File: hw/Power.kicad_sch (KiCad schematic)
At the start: 3 parts, among them Q2 SK2302AAT, SW4 SW_SPDT

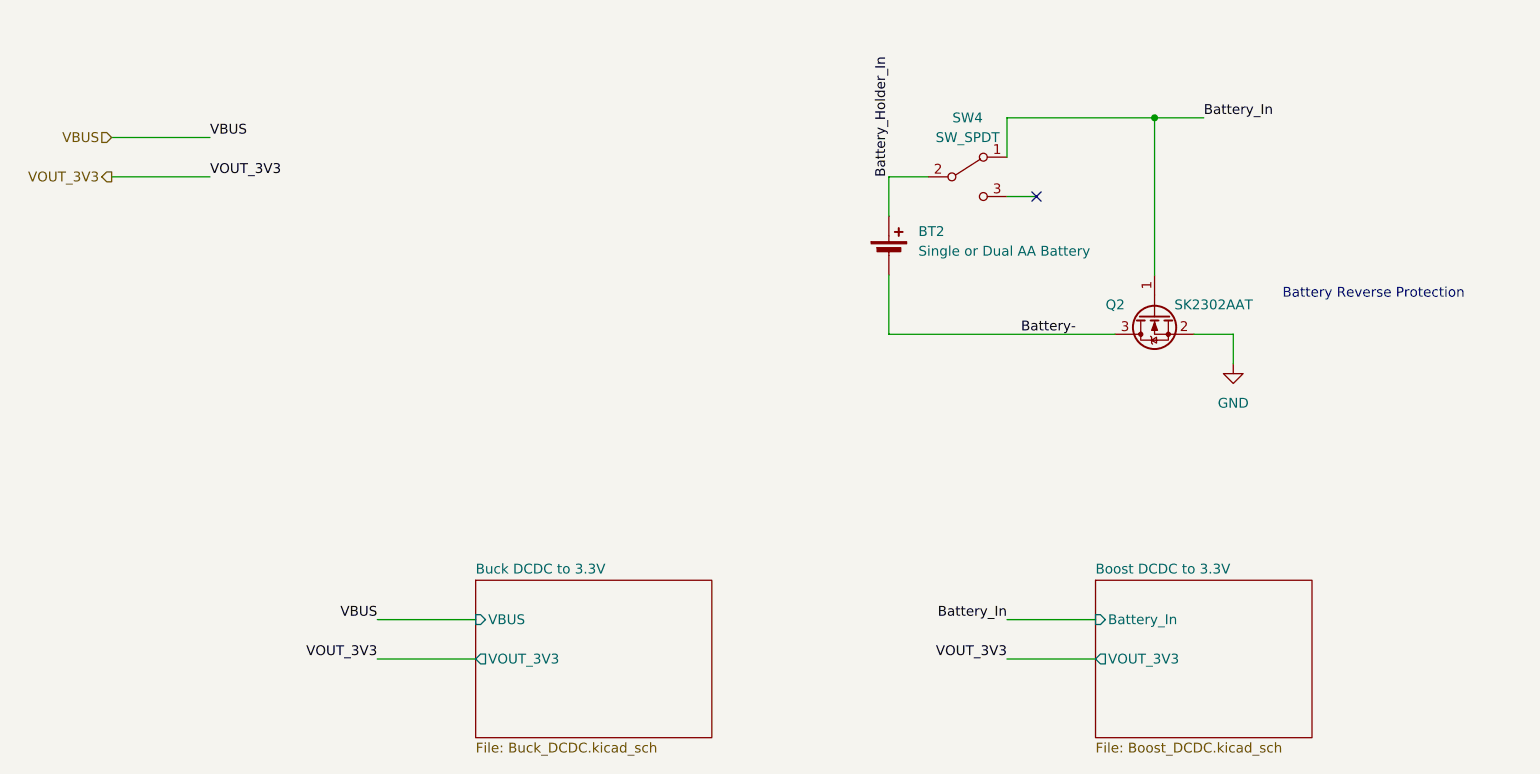
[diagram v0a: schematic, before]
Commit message: wired Battery measurement to ADC
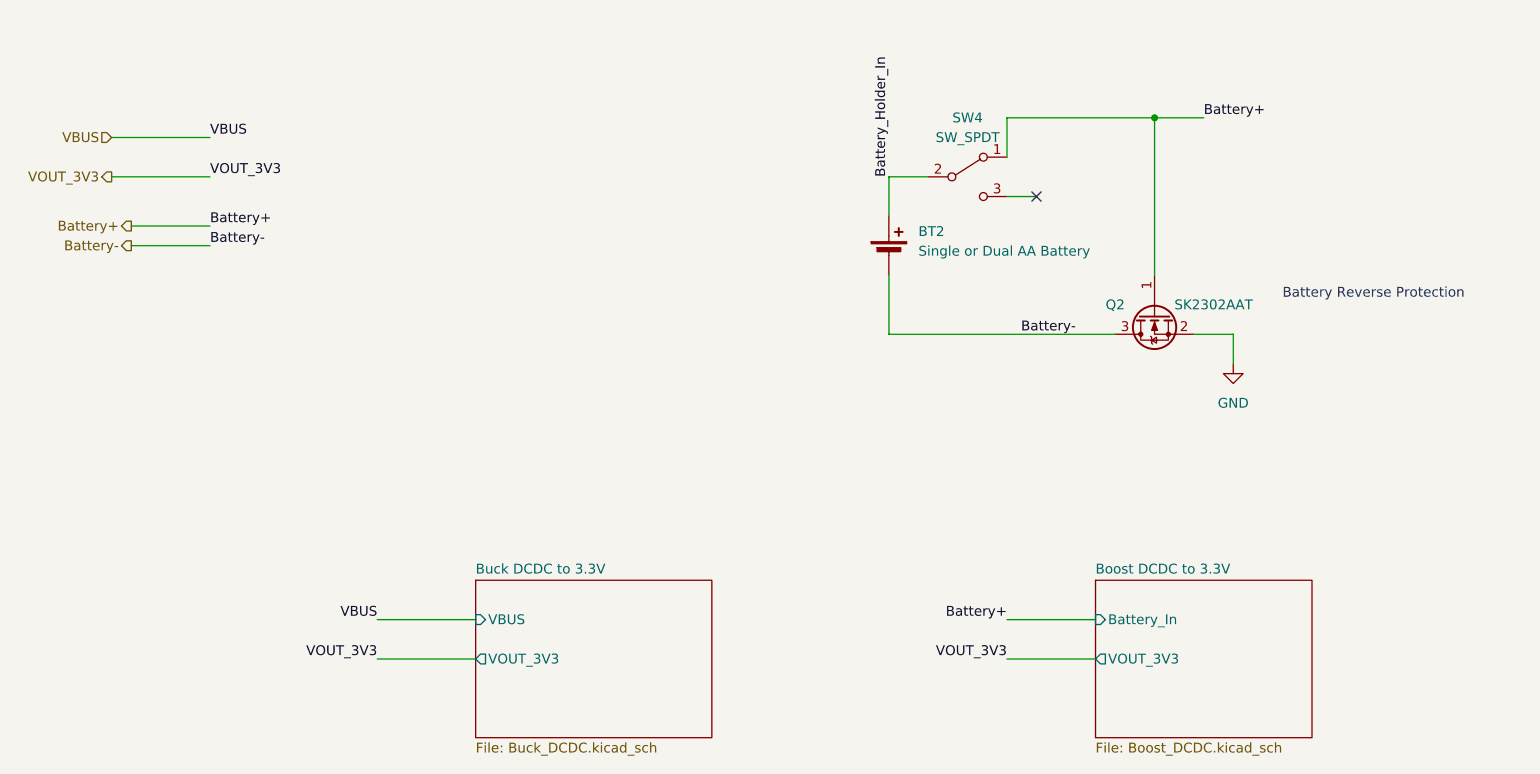
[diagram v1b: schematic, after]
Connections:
- net Battery_In renamed Battery+
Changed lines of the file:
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@@
+    (stroke (width 0) (type default))
+  )
+  (wire (pts (xy 45.72 41.91) (xy 55.88 41.91))
+    (stroke (width 0) (type default))
+  )
+  (wire (pts (xy 45.72 44.45) (xy 55.88 44.45))
     (stroke (width 0) (type default))
   )
@@
     (effects (font (size 1.27 1.27)) (justify left bottom))
   )
-  (label "Battery_In" (at 158.75 92.71 180) (fields_autoplaced)
+  (label "Battery+" (at 158.75 92.71 180) (fields_autoplaced)
     (effects (font (size 1.27 1.27)) (justify right bottom))
   )
@@
     (effects (font (size 1.27 1.27)) (justify right bottom))
   )
-  (label "Battery_In" (at 184.15 27.94 0) (fields_autoplaced)
+  (label "Battery+" (at 184.15 27.94 0) (fields_autoplaced)
+    (effects (font (size 1.27 1.27)) (justify left bottom))
+  )
+  (label "Battery-" (at 55.88 44.45 0) (fields_autoplaced)
     (effects (font (size 1.27 1.27)) (justify left bottom))
   )
   (label "Battery-" (at 167.64 55.88 180) (fields_autoplaced)
     (effects (font (size 1.27 1.27)) (justify right bottom))
+  )
+  (label "Battery+" (at 55.88 41.91 0) (fields_autoplaced)
+    (effects (font (size 1.27 1.27)) (justify left bottom))
   )
   (label "Battery_Holder_In" (at 143.51 35.56 90) (fields_autoplaced)
@@
     (effects (font (size 1.27 1.27)) (justify right bottom))
   )
+  (hierarchical_label "Battery+" (shape output) (at 45.72 41.91 180) (fields_autoplaced)
+    (effects (font (size 1.27 1.27)) (justify right))
+  )
   (hierarchical_label "VOUT_3V3" (shape output) (at 43.18 35.56 180) (fields_autoplaced)
     (effects (font (size 1.27 1.27)) (justify right))
@@
     (effects (font (size 1.27 1.27)) (justify right))
   )
+  (hierarchical_label "Battery-" (shape output) (at 45.72 44.45 180) (fields_autoplaced)
+    (effects (font (size 1.27 1.27)) (justify right))
+  )

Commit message: filled in LCSC
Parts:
- BT2: Vendor Model (none) -> BH-AA-A1AJ020
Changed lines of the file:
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@@
+      (effects (font (size 1.27 1.27)) hide)
+    )
+    (property "Vendor Model" "BH-AA-A1AJ020" (at 143.51 45.72 0)
       (effects (font (size 1.27 1.27)) hide)
     )
